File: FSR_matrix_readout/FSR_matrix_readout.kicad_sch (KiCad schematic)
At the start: 2 parts

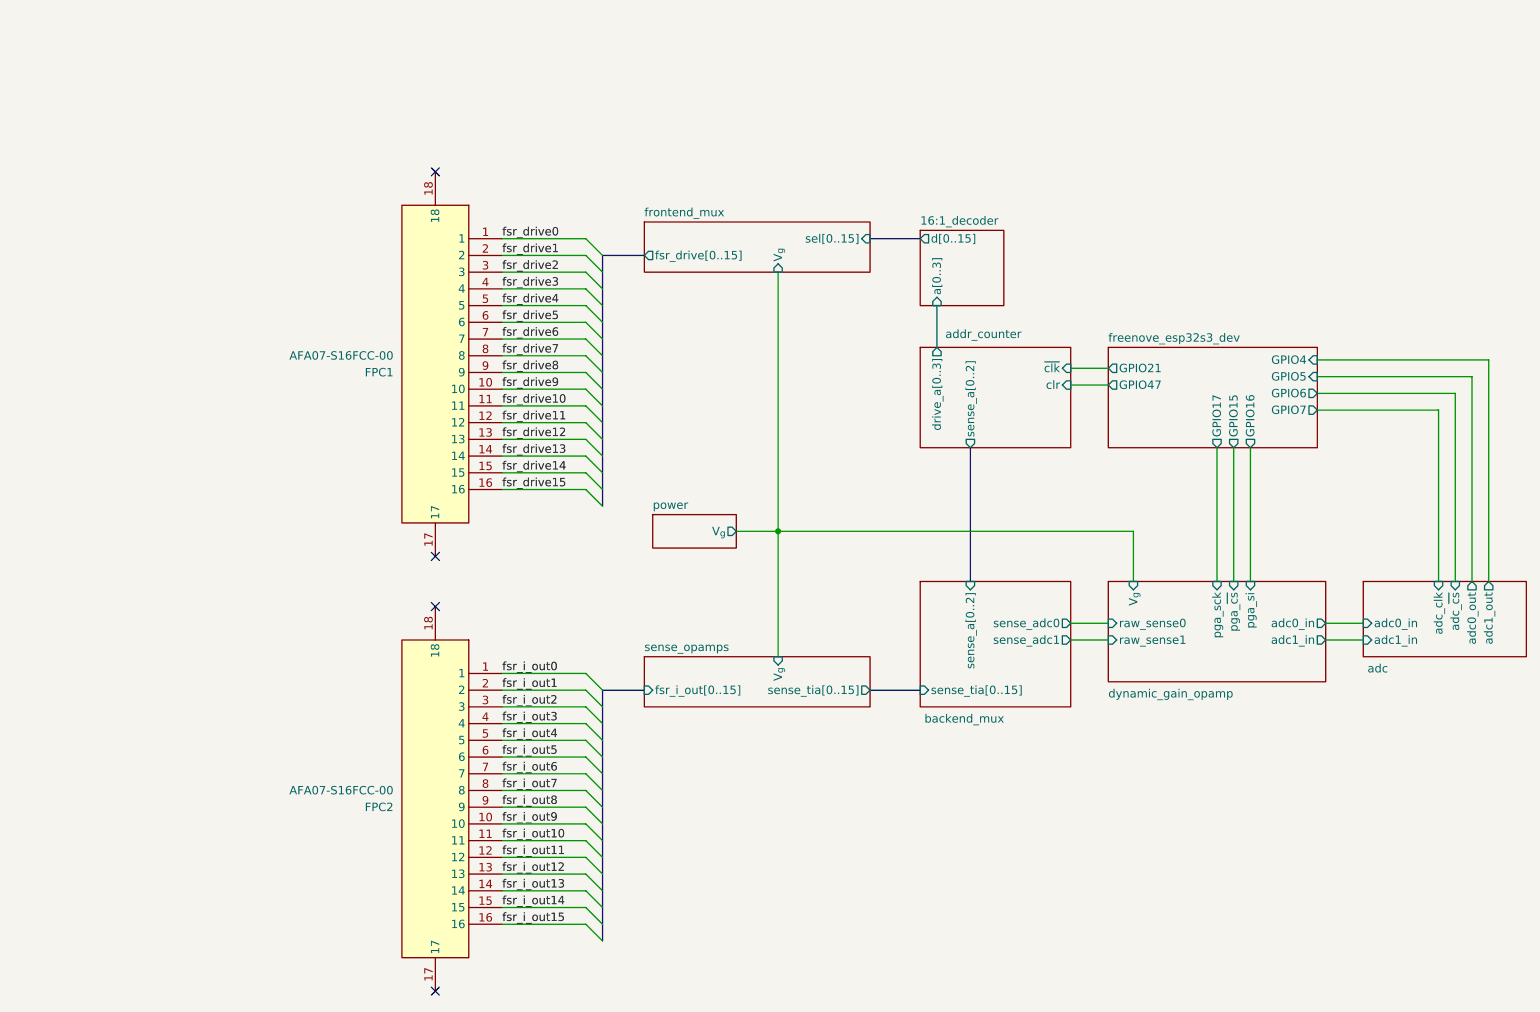
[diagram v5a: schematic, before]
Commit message: remove all ERC errors
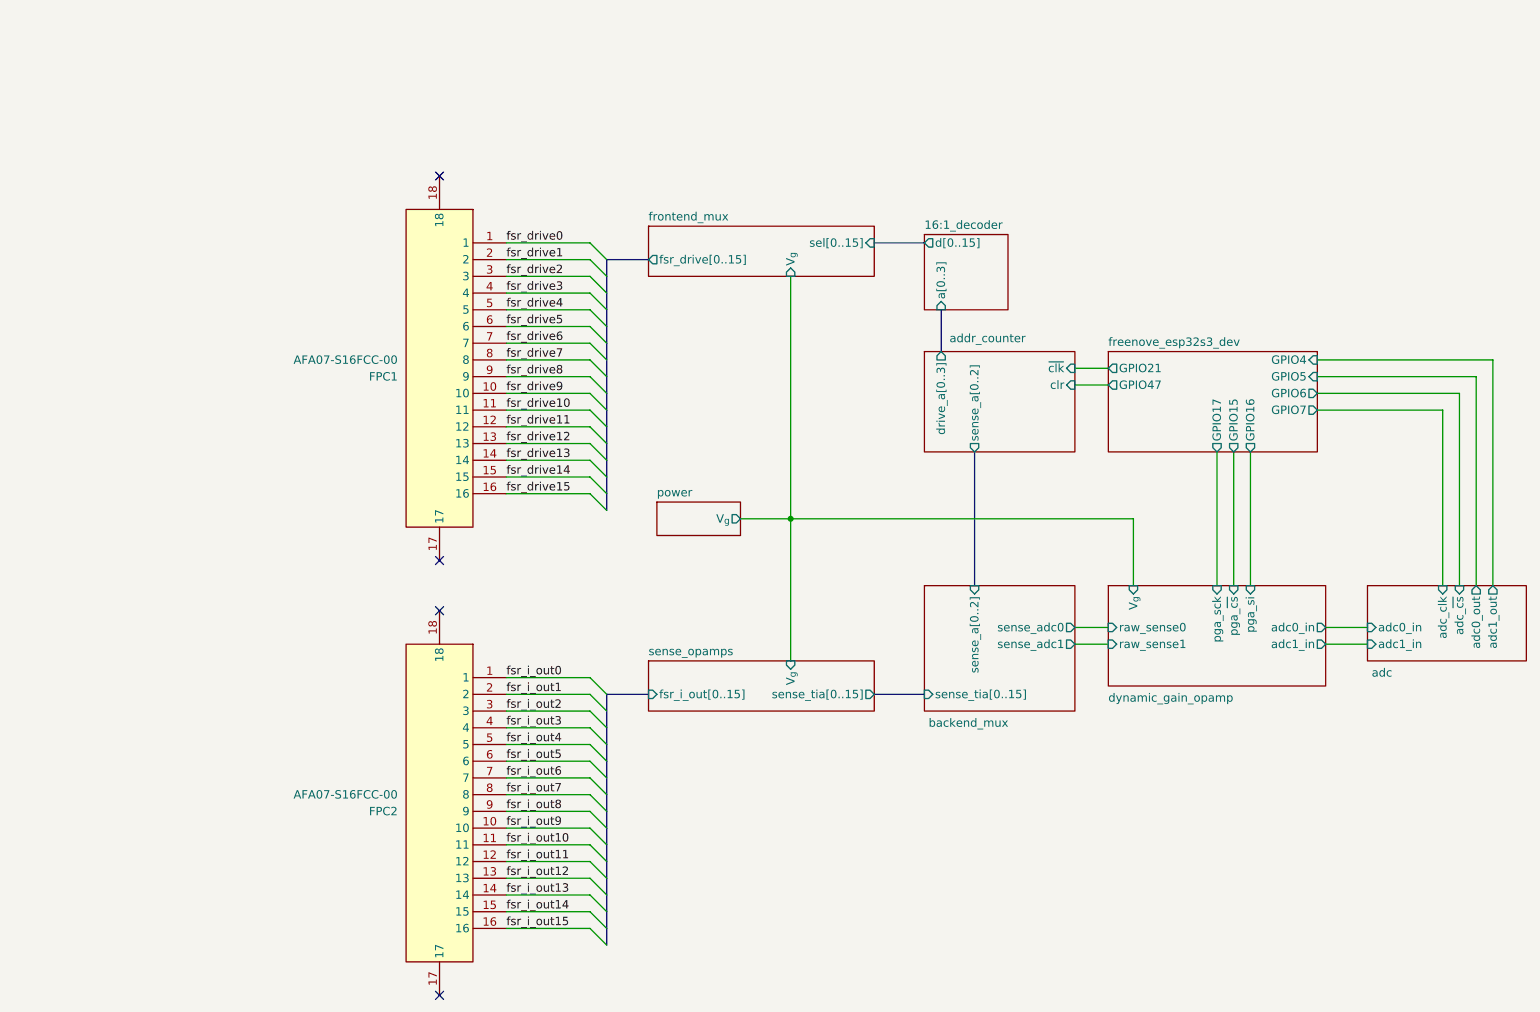
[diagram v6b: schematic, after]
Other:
- moved on the sheet: FPC1, FPC2
